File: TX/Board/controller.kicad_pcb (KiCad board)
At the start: 2 copper layers, 31.8 x 76.5 mm, 15 parts, among them J1 CONN_SWITCH, J2 PROG_CONN, J3 RX_JMP, J4 TX_JMP, J5 AT_MODE_JUMP, J6 BATT_CONN, J7 GENERIC, U1 ARDUINO_PRO_MINI, U2 ITEAD_HC-05

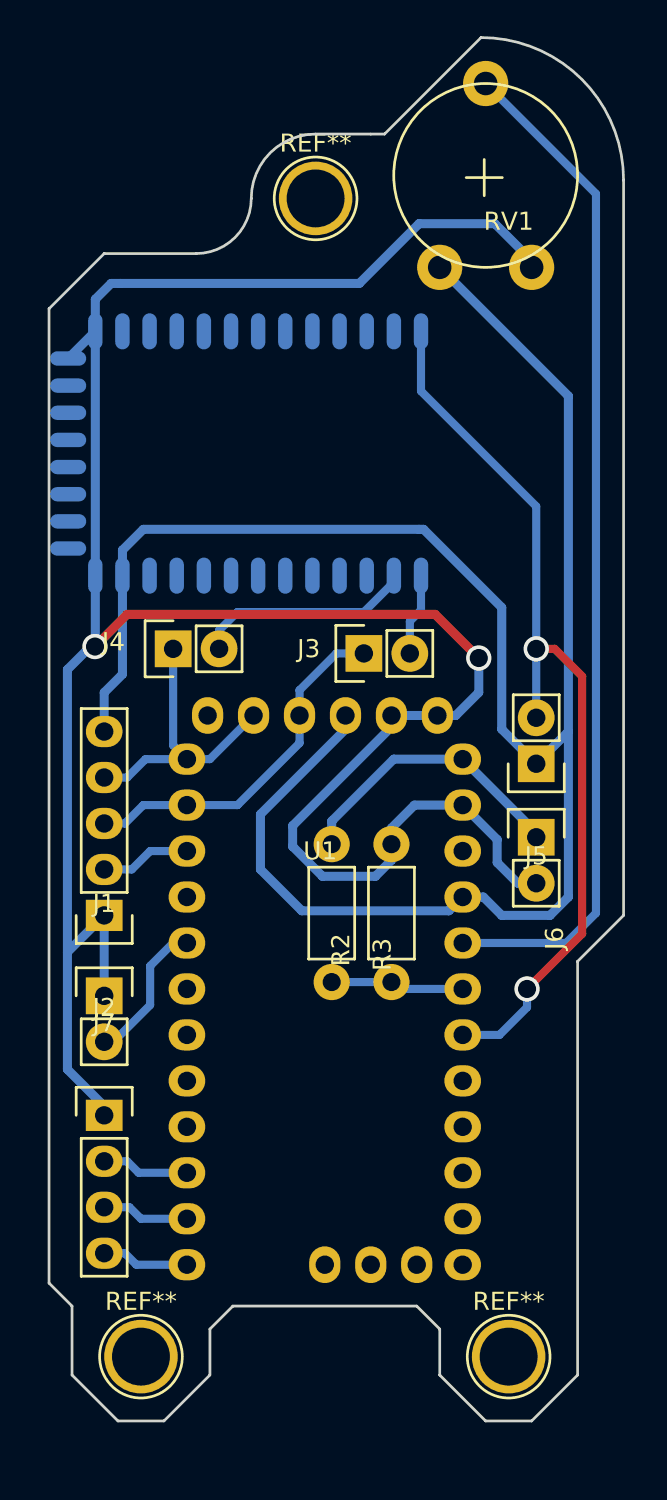
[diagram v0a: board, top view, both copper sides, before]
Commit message: Corrected bugs and added first prototype of receiver board
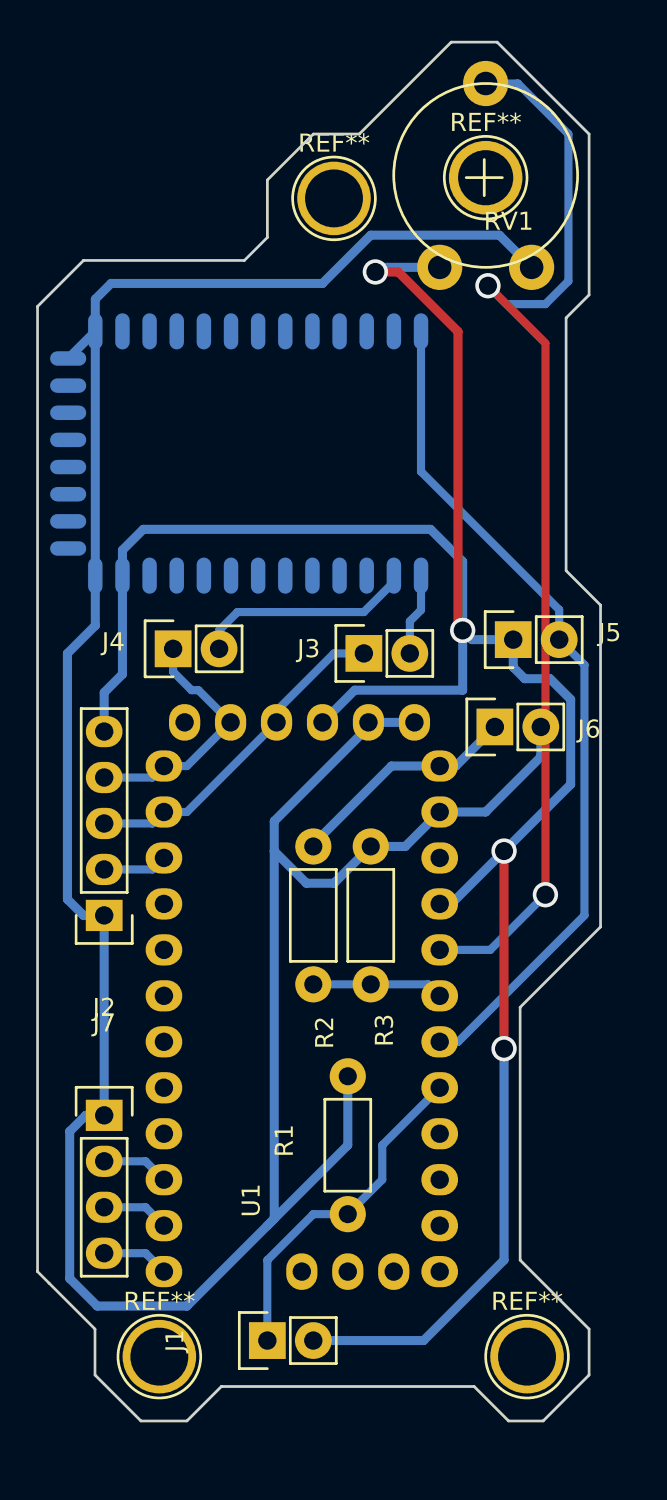
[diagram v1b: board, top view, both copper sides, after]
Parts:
- added R1: R, Resistors_THT:Resistor_Horizontal_RM7mm, F.Cu at (160.0, 148.1)
- added REF**: 1pin, Connect:1pin, F.Cu at (167.6, 90.8)
- J1: value CONN_SWITCH -> PRESENCE_SENS
- moved J1 21.1 mm to (155.6, 155.1), turned to 90 degrees
- moved J5 6.97 mm to (169.2, 116.3), turned to 90 degrees
- moved J6 6.51 mm to (168.1, 121.2), turned to 90 degrees
- moved U1 1.33 mm to (157.5, 120.8)
- moved R3 1.15 mm to (161.3, 135.4)
- moved R2 1.02 mm to (158.1, 127.8)
- moved REF** 1.02 mm to (159.3, 91.9)
- moved REF** 1.02 mm to (149.6, 156.0)
- moved REF** 1.02 mm to (169.9, 156.0)
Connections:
- J1 pad 1: GNDREF -> PRESENCE_SENSOR
- J1 pad 2: SWITCH_PRESENZA -> +3V3
- U1 pad 20: (no net) -> PRESENCE_SENSOR
- U1 pad 5: SWITCH_PRESENZA -> (no net)
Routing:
- net GNDREF: track 142.3 -> 162.3 mm, vias 2 -> 0
- net PRESENCE_SENSOR: track 0.00 -> 19.0 mm
- net +3V3: track 112.9 -> 130.4 mm, vias 0 -> 4
- net SWITCH_PRESENZA: track 8.10 -> 0.00 mm
- net ACCEL_POT: track 56.4 -> 61.3 mm, vias 0 -> 2
- net AT_MODE: track 50.9 -> 46.9 mm, vias 2 -> 0
- net +BATT: track 15.9 -> 12.8 mm
- net TX_ARD: track 16.1 -> 13.8 mm
- net RST_ARD: track 4.99 -> 3.57 mm
- net RX_ARD: track 20.0 -> 18.6 mm
- net G3: track 4.84 -> 3.72 mm
- net G2: track 4.84 -> 3.72 mm
- net G1: track 4.84 -> 3.72 mm
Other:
- board size 31.8 x 76.5 mm -> 31.1 x 76.2 mm

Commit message: Added low-pass filter to the transmitter -> stable acc reading
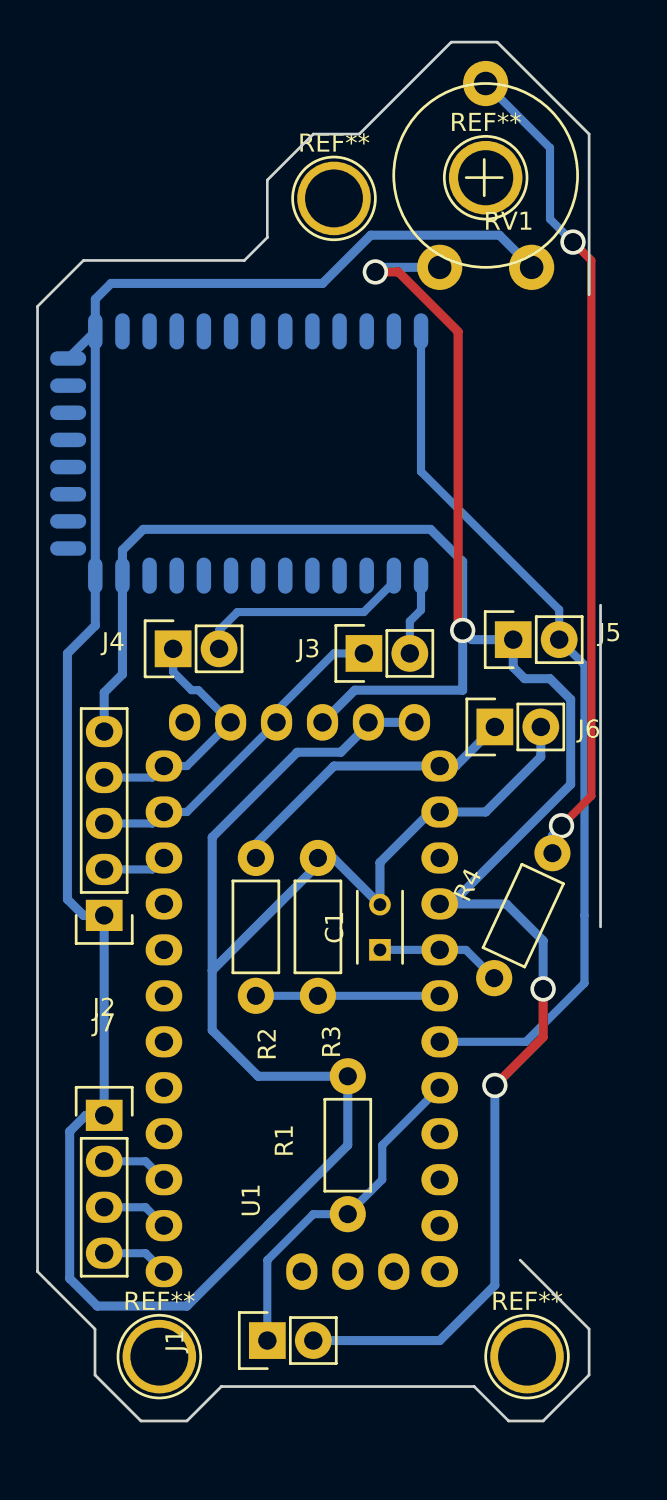
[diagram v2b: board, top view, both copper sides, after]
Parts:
- added C1: 1uF, Capacitors_THT:C_Rect_L4_W2.5_P2.5, F.Cu at (161.8, 133.5)
- added R4: 3k3, Resistors_THT:Resistor_Horizontal_RM7mm, F.Cu at (168.1, 135.0)
- moved R2 3.24 mm to (154.9, 128.4)
- moved R3 2.99 mm to (158.4, 136.0)
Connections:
- RV1 pad 2: ACCEL_POT -> Net-(R4-Pad2)
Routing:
- net ACCEL_POT: track 61.3 -> 6.96 mm, vias 2 -> 0
- net Net-(R4-Pad2): track 0.00 -> 45.8 mm, vias 0 -> 2
- net GNDREF: track 162.3 -> 171.6 mm
- net +BATT: track 12.8 -> 16.7 mm
- net +3V3: track 130.4 -> 133.4 mm
- net BATT_SENS: track 7.25 -> 10.2 mm
- net AT_MODE: track 46.9 -> 49.1 mm
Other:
- outline, holes or cut-outs redrawn

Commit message: Added images and first version of the led panel
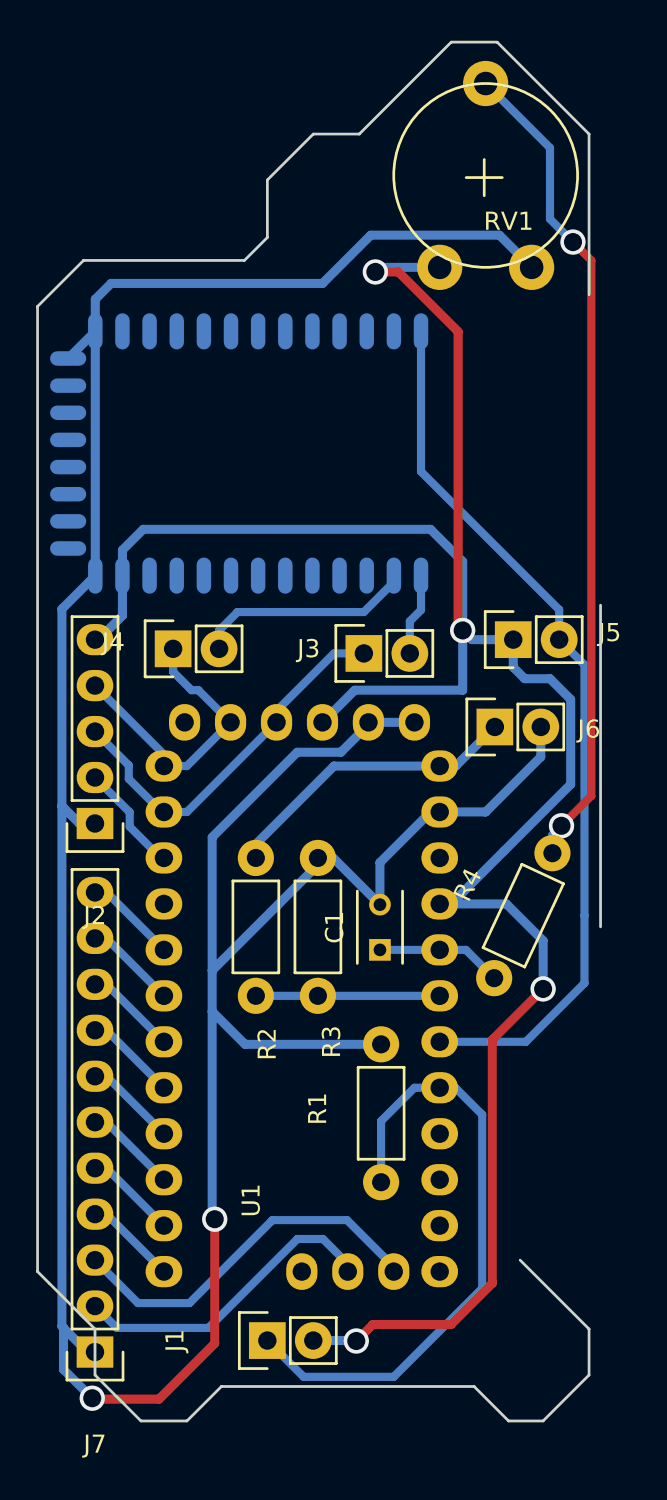
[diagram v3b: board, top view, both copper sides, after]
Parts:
- removed REF** (x4): 1pin, Connect:1pin
- J7: value GENERIC -> LED_SPEED; footprint Pin_Headers:Pin_Header_Straight_1x04 -> Pin_Headers:Pin_Header_Straight_1x11
- moved J7 13.1 mm to (146.1, 155.7), turned to 180 degrees
- moved J2 5.11 mm to (146.1, 126.5)
- moved R1 2.55 mm to (161.9, 146.3)
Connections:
- net G1 renamed SPLED_2
- J7 pad 2: G3 -> SPLED_0
- J7 pad 3: G2 -> SPLED_1
- R3 pad 2: GNDREF -> (no net)
- U1 pad 10: G3 -> SPLED_4
- U1 pad 11: G2 -> SPLED_3
- U1 pad 14: (no net) -> SPLED_0
- U1 pad 15: (no net) -> SPLED_1
- U1 pad 5: (no net) -> SPLED_9
- U1 pad 6: (no net) -> SPLED_8
- U1 pad 7: (no net) -> SPLED_7
- U1 pad 8: (no net) -> SPLED_6
- U1 pad 9: (no net) -> SPLED_5
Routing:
- net SPLED_1: track 0.00 -> 20.7 mm
- net SPLED_0: track 0.00 -> 17.5 mm
- net PRESENCE_SENSOR: track 19.0 -> 34.7 mm
- net GNDREF: track 171.6 -> 183.6 mm, vias 0 -> 2
- net SPLED_9: track 0.00 -> 5.13 mm
- net SPLED_6: track 0.00 -> 5.13 mm
- net SPLED_5: track 0.00 -> 5.13 mm
- net SPLED_3: track 0.00 -> 5.13 mm
- net SPLED_8: track 0.00 -> 5.13 mm
- net SPLED_7: track 0.00 -> 5.13 mm
- net SPLED_4: track 0.00 -> 5.13 mm
- net +3V3: track 133.4 -> 128.5 mm
- net G2: track 3.72 -> 0.00 mm
- net G3: track 3.72 -> 0.00 mm
- net RST_ARD: track 3.57 -> 6.12 mm
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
